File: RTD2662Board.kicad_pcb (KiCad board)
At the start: 2 copper layers, 100 x 65 mm, 227 parts, among them J1 USB_B, J10 Conn_Coaxial, J11 Conn_01x03, J2 AudioJack4, J3 Jack, J4 Conn_02x25_Odd_Even, J5 AudioJack4, J6 DVI_FEMALE, J7 HDMI_A_1.4, J8 Mini-DIN-4, J9 DB15_Female_HighDensity_Mount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, Q5 BC846, Q7 AO3401A, Q8 BC846, Q9 BC846, SW1 SW_Push, SW2 SW_Push, SW3 SW_Push, SW4 SW_Push, SW5 SW_Push, U1 TSOP382xx, U10 TPS61040DBV, U11 TPS61040DBV, U12 CH341T, U2 ES7134S, U4 PAM8003, U5 TPS61040DBV, U6 APW7313, U7 AMS1117-1.8, U8 RTD2662, U9 W25Qxx, Y1 Crystal, Y2 Crystal

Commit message: Revision 0.2
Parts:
- removed Q5: BC846, Package_TO_SOT_SMD:SOT-23
- removed R89: R, Resistor_SMD:R_0402_1005Metric_Pad0.72x0.64mm_HandSolder
- added C58: C, Capacitor_SMD:C_0402_1005Metric_Pad0.74x0.62mm_HandSolder, F.Cu at (112.2, 105.5)
- added C59: C, Capacitor_SMD:C_0402_1005Metric_Pad0.74x0.62mm_HandSolder, F.Cu at (106.2, 105.5)
- added C68: C, Capacitor_SMD:C_0402_1005Metric_Pad0.74x0.62mm_HandSolder, F.Cu at (133.0, 95.2)
- added C69: C, Capacitor_SMD:C_0402_1005Metric_Pad0.74x0.62mm_HandSolder, F.Cu at (130.2, 91.0)
- added C70: C, Capacitor_SMD:C_0402_1005Metric_Pad0.74x0.62mm_HandSolder, F.Cu at (132.2, 93.2)
- added C71: C, Capacitor_SMD:C_0402_1005Metric_Pad0.74x0.62mm_HandSolder, F.Cu at (131.5, 95.2)
- added C72: C, Capacitor_SMD:C_0402_1005Metric_Pad0.74x0.62mm_HandSolder, F.Cu at (36.5, 98.5)
- added C73: C, Capacitor_SMD:C_0402_1005Metric_Pad0.74x0.62mm_HandSolder, F.Cu at (87.5, 101.8)
- added C75: C, Capacitor_SMD:C_0402_1005Metric_Pad0.74x0.62mm_HandSolder, F.Cu at (36.5, 99.8)
- added C76: C, Capacitor_SMD:C_0402_1005Metric_Pad0.74x0.62mm_HandSolder, F.Cu at (87.6, 113.8)
- added C77: C, Capacitor_SMD:C_0402_1005Metric_Pad0.74x0.62mm_HandSolder, F.Cu at (36.4, 97.2)
- added C78: C, Capacitor_SMD:C_0402_1005Metric_Pad0.74x0.62mm_HandSolder, F.Cu at (36.4, 101.0)
- added C80: C, Capacitor_SMD:C_0402_1005Metric_Pad0.74x0.62mm_HandSolder, F.Cu at (78.2, 105.2)
- added D24: D_TVS, Inductor_SMD:L_0402_1005Metric_Pad0.77x0.64mm_HandSolder, F.Cu at (130.2, 88.0)
- added FB10: 120Ω, Inductor_SMD:L_0402_1005Metric_Pad0.77x0.64mm_HandSolder, F.Cu at (132.2, 87.2)
- added J12: Conn_02x06_Odd_Even, Connector_PinHeader_2.54mm:PinHeader_2x06_P2.54mm_Vertical, F.Cu at (127.0, 115.8)
- added J13: Conn_01x10, Connector_JST:JST_PH_B10B-PH-K_1x10_P2.00mm_Vertical, F.Cu at (56.8, 80.0)
- added J14: Conn_01x02, Connector_PinHeader_2.54mm:PinHeader_1x02_P2.54mm_Vertical, F.Cu at (144.8, 81.8)
- added J15: Conn_01x02, Connector_PinHeader_2.54mm:PinHeader_1x02_P2.54mm_Vertical, F.Cu at (75.2, 97.5)
- added JP5: Reset Pad, Jumper:SolderJumper-2_P1.3mm_Open_Pad1.0x1.5mm, F.Cu at (90.8, 118.8)
- added JP6: Power select, Connector_PinSocket_2.54mm:PinSocket_1x03_P2.54mm_Vertical, F.Cu at (60.0, 100.0)
- added JP7: Jump, Jumper:SolderJumper-2_P1.3mm_Bridged2Bar_RoundedPad1.0x1.5mm, B.Cu at (78.5, 92.0)
- added L8: L, Inductor_SMD:L_0402_1005Metric_Pad0.77x0.64mm_HandSolder, F.Cu at (132.2, 91.8)
- added Q1: AO3401A, Package_TO_SOT_SMD:SOT-23, F.Cu at (97.0, 79.0)
- added Q2: BC846, Package_TO_SOT_SMD:SOT-23, F.Cu at (101.5, 79.0)
- added R28: R, Resistor_SMD:R_0402_1005Metric_Pad0.72x0.64mm_HandSolder, F.Cu at (128.5, 90.2)
- added R30: R, Resistor_SMD:R_0402_1005Metric_Pad0.72x0.64mm_HandSolder, F.Cu at (127.0, 90.2)
- added R31: R, Resistor_SMD:R_0402_1005Metric_Pad0.72x0.64mm_HandSolder, F.Cu at (127.0, 93.2)
- added R36: R, Resistor_SMD:R_0402_1005Metric_Pad0.72x0.64mm_HandSolder, F.Cu at (128.5, 93.2)
- added R38: R, Resistor_SMD:R_0402_1005Metric_Pad0.72x0.64mm_HandSolder, F.Cu at (104.5, 80.0)
- added R40: R, Resistor_SMD:R_0402_1005Metric_Pad0.72x0.64mm_HandSolder, F.Cu at (132.2, 90.2)
- added R42: R, Resistor_SMD:R_0402_1005Metric_Pad0.72x0.64mm_HandSolder, F.Cu at (104.5, 78.2)
- added R78: 75Ω, Resistor_SMD:R_0402_1005Metric_Pad0.72x0.64mm_HandSolder, F.Cu at (132.2, 88.8)
- added R85: R, Resistor_SMD:R_0402_1005Metric_Pad0.72x0.64mm_HandSolder, F.Cu at (78.5, 87.0)
- added U3: AT24CS08-STUM, Package_TO_SOT_SMD:SOT-23-5, F.Cu at (127.8, 96.5)
- C52, C53, C54, C9: footprint Capacitor_SMD:C_0402_1005Metric_Pad0.74x0.62mm_HandSolder -> Capacitor_SMD:C_0805_2012Metric_Pad1.18x1.45mm_HandSolder
- JP1, JP2, JP3, JP4: moved to B.Cu
- R81: footprint Resistor_SMD:R_0402_1005Metric_Pad0.72x0.64mm_HandSolder -> Resistor_SMD:R_1210_3225Metric_Pad1.30x2.65mm_HandSolder
- SW1: value SW_Push -> POWER
- SW2: value SW_Push -> MENU
- SW3: value SW_Push -> UP
- SW4: value SW_Push -> DOWN
- SW5: value SW_Push -> SOURCE
- U9: footprint Package_SO:SOIC-8_3.9x4.9mm_P1.27mm -> Package_DIP:DIP-8_W7.62mm_Socket
- moved C9 24.0 mm to (55.8, 92.5), turned to 90 degrees
- moved R12 20.1 mm to (76.0, 87.0), turned to 90 degrees
- moved R20 18.6 mm to (71.0, 87.0), turned to 270 degrees
- moved R14 18.3 mm to (77.2, 87.0)
- moved R1 17.7 mm to (72.2, 87.0), turned to 90 degrees
- moved R8 17.7 mm to (74.8, 87.0), turned to 90 degrees
- moved R5 15.3 mm to (73.5, 87.0), turned to 90 degrees
- moved U7 13.5 mm to (61.5, 93.8)
- moved C39 13.0 mm to (94.2, 119.2), turned to 90 degrees
- moved R81 11.1 mm to (114.2, 84.5)
- moved JP3 10.0 mm to (92.8, 79.2), turned to 90 degrees
- moved JP4 9.80 mm to (92.8, 83.8)
- moved R9 9.63 mm to (120.6, 102.8), turned to 0 degrees
- moved R61 9.25 mm to (93.0, 119.2), turned to 270 degrees
- moved R76 8.68 mm to (103.5, 87.0)
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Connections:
- net CVBS+ renamed CVBS0+
- net CVBS- renamed CVBS0-
- net I2S_SDAT renamed I2S_SDAT0
- net Net-(U8-Pad114) renamed I2S_SDAT3
- net _CVBS+ renamed _CVBS0+
- net _CVBS- renamed _CVBS0-
- C50 pad 1: GND -> AVCC
- C51 pad 1: GND -> AVCC
- D21 pad 1: GND -> AVCC
- D22 pad 2: GND -> AVCC
- J1 pad 1: Net-(J1-Pad1) -> VUSB
- J4 pad 49: Net-(J4-Pad49) -> EN_LCD
- J4 pad 50: Net-(J4-Pad50) -> EN_BL
- JP3 pad 1: +3V3 -> Net-(JP3-Pad1)
- Q7 pad 3: Net-(J3-Pad1) -> Net-(JP6-Pad2)
- R1 pad 1: Net-(R1-Pad1) -> BUTTONS
- R1 pad 2: GND -> MENUB
- R10 pad 1: RED_LED -> GRN_LED
- R12 pad 1: Net-(R12-Pad1) -> BUTTONS
- R12 pad 2: GND -> SRCB
- R13 pad 1: GRN_LED -> RED_LED
- R14 pad 1: +3V3 -> Net-(J13-Pad9)
- R14 pad 2: Net-(Q5-Pad3) -> RED_LED
- R17 pad 1: Net-(Q5-Pad1) -> Net-(C73-Pad1)
- R5 pad 1: Net-(R5-Pad1) -> BUTTONS
- R5 pad 2: GND -> UPB
- R8 pad 1: Net-(R8-Pad1) -> BUTTONS
- R8 pad 2: GND -> DWNB
- R88 pad 1: EN_REF -> EN_LCD
- SW1 pad 1: Net-(R1-Pad1) -> GND
- SW2 pad 1: Net-(R5-Pad1) -> GND
- SW2 pad 2: BUTTONS -> MENUB
- SW3 pad 1: Net-(R8-Pad1) -> GND
- SW3 pad 2: BUTTONS -> UPB
- SW4 pad 1: Net-(R12-Pad1) -> GND
- SW4 pad 2: BUTTONS -> DWNB
- SW5 pad 2: BUTTONS -> SRCB
- U10 pad 4: EN_REF -> EN_LCD
- U11 pad 4: EN_REF -> EN_LCD
- U4 pad 12: Net-(Q5-Pad3) -> Net-(C73-Pad1)
- U4 pad 2: Net-(J2-PadS) -> Net-(J2-PadR2)
- U8 pad 100: VOL -> EN_LCD
- U8 pad 102: Net-(U8-Pad102) -> VOL
- U8 pad 112: Net-(U8-Pad112) -> I2S_SDAT1
- U8 pad 113: Net-(U8-Pad113) -> I2S_SDAT2
- U8 pad 47: Net-(U8-Pad47) -> CVBS1+
- U8 pad 48: Net-(U8-Pad48) -> CVBS1-
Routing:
- net GND: track 682.3 -> 26.4 mm, vias 308 -> 16
- net +1V8: track 146.8 -> 41.3 mm, vias 5 -> 0
- net IRDA: track 79.7 -> 13.9 mm, vias 2 -> 0
- net VCOM: track 32.3 -> 97.2 mm, vias 0 -> 2
- net BUTTONS: track 102.6 -> 39.7 mm
- net TX: track 116.2 -> 56.6 mm
- net RX: track 124.3 -> 65.4 mm
- net +3V3: track 398.9 -> 358.7 mm
- net EN_LCD: track 0.00 -> 36.9 mm
- net I2S_SDAT1: track 0.00 -> 35.5 mm, vias 0 -> 1
- net CVBS1+: track 0.00 -> 34.9 mm
- net EIO6: track 0.00 -> 34.0 mm, vias 0 -> 1
- net CVBS1-: track 0.00 -> 33.5 mm
- net I2S_SDAT2: track 0.00 -> 33.0 mm, vias 0 -> 1
- net EIO7: track 0.00 -> 31.4 mm, vias 0 -> 1
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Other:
- board size 100 x 65 mm -> 100 x 70 mm
- net class LCD Signal removed
- net class Power added: clearance 0.2, trace_width 0.75, via_dia 0.8, via_drill 0.4

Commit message: Revision 1.0
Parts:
- removed C78, C80: C, Capacitor_SMD:C_0402_1005Metric_Pad0.74x0.62mm_HandSolder
- removed the J6 at (90.2, 142.5)
- removed the R9 at (120.6, 102.8)
- removed the U9 at (83.5, 118.2)
- added C65: C, Capacitor_SMD:C_0402_1005Metric_Pad0.74x0.62mm_HandSolder, F.Cu at (78.2, 104.8)
- added J1: DVI_Female, RTD2662Board:DVI, F.Cu at (90.2, 142.5)
- added R57: R, Resistor_SMD:R_0402_1005Metric_Pad0.72x0.64mm_HandSolder, F.Cu at (125.0, 84.8)
- added R87: R, Resistor_SMD:R_0402_1005Metric_Pad0.72x0.64mm_HandSolder, F.Cu at (62.8, 119.5)
- added U10: W25Qxx, RTD2662Board:SOIC-8_3.9x4.9mm_P1.27mm_DIP-8_W7.62mm_Socket, F.Cu at (79.6, 113.2)
- D22: renamed from D2; value LED_Dual_ACAC -> Dual LED
- J10: renamed from J11; value Conn_01x03 -> UART/I2C
- J11: renamed from J4; value Conn_02x25_Odd_Even -> LCD Connector
- J12: renamed from J15; value Conn_01x02 -> SPDIFF
- J15: renamed from J12; value Conn_02x06_Odd_Even -> Expansion Connector
- J9: renamed from J13; value Conn_01x10 -> Keyboard Connector
- JP4: footprint Jumper:SolderJumper-2_P1.3mm_Bridged2Bar_RoundedPad1.0x1.5mm -> Jumper:SolderJumper-2_P1.3mm_Open_RoundedPad1.0x1.5mm
- moved C61 91.3 mm to (127.8, 97.8)
- moved C64 52.6 mm to (88.5, 90.0), turned to 180 degrees
- moved JP7 44.9 mm to (58.8, 87.2), turned to 180 degrees
- moved C69 43.9 mm to (64.2, 87.2)
- moved R84 42.2 mm to (65.5, 87.2)
- moved C62 31.9 mm to (67.2, 108.2)
- moved R77 27.5 mm to (78.5, 90.0), turned to 270 degrees
- moved R80 25.0 mm to (77.2, 90.0), turned to 270 degrees
- moved REF** 13.5 mm to (52.8, 96.2)
- moved Q4 9.36 mm to (100.0, 88.2)
- moved C37 9.33 mm to (109.8, 86.8)
- moved C38 9.33 mm to (108.2, 86.8)
- moved C43 9.33 mm to (121.0, 86.8)
- moved C44 9.33 mm to (122.5, 86.8)
- moved D17 9.33 mm to (108.2, 89.2)
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- renumbered C36 to C1, C17 to C10, C69 to C11, C70 to C12, C19 to C13, C20 to C14, C71 to C15, C22 to C16, C26 to C17, C28 to C18, C31 to C19, C12 to C2, C30 to C20, C29 to C21, C32 to C22, C27 to C23, C16 to C24, C35 to C25, C18 to C26, C34 to C27, C21 to C28, C33 to C29, C41 to C3, C23 to C30, C45 to C31, C24 to C32, C43 to C33, C25 to C34, C40 to C35, C46 to C36, C47 to C37, C48 to C38, C52 to C39, C42 to C4, C37 to C40, C38 to C41, C49 to C42, C50 to C43, C51 to C44, C53 to C45, C1 to C46, C2 to C47, C4 to C48, C5 to C49, C13 to C5, C3 to C50, C54 to C51, C73 to C52, C6 to C53, C57 to C54, C60 to C55, C63 to C56, C64 to C57, C65 to C58, C66 to C59, C14 to C6, C67 to C60, C72 to C61, C75 to C62, C76 to C63, C77 to C64, C7 to C66, C8 to C67, C9 to C68, C39 to C69, C44 to C7, C55 to C70, C56 to C71, C59 to C72, C58 to C73, C62 to C74, C61 to C75, C10 to C76, C11 to C77, C15 to C8, C68 to C9, D12 to D1, D13 to D10, D14 to D11, D15 to D12, D16 to D13, D17 to D14, D20 to D15, D18 to D16, D19 to D17, D1 to D18, D21 to D19, D4 to D2, D22 to D20, D23 to D21, D11 to D23, D3 to D24, D24 to D3, D6 to D4, D9 to D5, D8 to D6, D5 to D7, D10 to D8, D7 to D9, FB8 to FB1, FB9 to FB10, FB1 to FB2, FB10 to FB3, FB3 to FB4, FB2 to FB7, FB7 to FB8, FB4 to FB9, J2 to J13, J3 to J14, J7 to J2, J5 to J3, J9 to J4, J10 to J5, J14 to J6, J8 to J7, J1 to J8, JP7 to JP5, JP5 to JP7, L5 to L1, L3 to L2, L8 to L3, L6 to L5, L1 to L6, L2 to L8, Q8 to Q1, Q9 to Q2, Q1 to Q3, Q2 to Q4, Q7 to Q5, R2 to R1, R34 to R10, R40 to R11, R37 to R12, R78 to R13, R41 to R14, R7 to R15, R15 to R16, R21 to R17, R27 to R18, R48 to R19, R4 to R2, R47 to R20, R49 to R21, R53 to R22, R57 to R23, R55 to R24, R54 to R25, R58 to R26, R52 to R27, R35 to R28, R64 to R29, R32 to R3, R39 to R30, R62 to R31, R43 to R32, R59 to R33, R50 to R34, R51 to R35, R44 to R36, R70 to R37, R56 to R38, R45 to R39, R16 to R4, R69 to R40, R46 to R41, R67 to R42, R71 to R43, R72 to R44, R63 to R45, R18 to R46, R73 to R47, R74 to R48, R76 to R49, R19 to R5, R77 to R50, R88 to R51, R60 to R52, R20 to R53, R75 to R54, R66 to R55, R1 to R56, R81 to R58, R11 to R59, R29 to R6, R5 to R60, R3 to R61, R8 to R62, R6 to R63, R79 to R64, R12 to R65, R82 to R66, R38 to R67, R14 to R68, R17 to R69, R65 to R7, R42 to R70, R80 to R71, R83 to R72, R84 to R73, R85 to R74, R28 to R75, R30 to R76, R10 to R77, R31 to R78, R36 to R79, R33 to R8, R13 to R80, R22 to R81, R23 to R82, R24 to R83, R61 to R84, R25 to R85, R26 to R86, R68 to R9, U8 to U1, U6 to U11, U7 to U12, U10 to U2, U1 to U3, U12 to U4, U2 to U6, U4 to U7, U11 to U8, U3 to U9, Y2 to Y1, Y1 to Y2
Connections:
- net Net-(C39-Pad1) renamed ~RESET~
- net Net-(J2-PadR1) renamed RIGHT+
- net Net-(J2-PadR2) renamed LEFT-
- net Net-(J2-PadS) renamed RIGHT-
- net Net-(J2-PadT) renamed LEFT+
- C11 pad 2: _CVBS1- -> GND
- C12 pad 2: _CVBS1- -> GND
- C13 pad 2: _S_Y- -> GND
- C14 pad 2: _S_Y- -> GND
- C15 pad 2: _CVBS1- -> GND
- C16 pad 2: _S_Y- -> GND
- C20 pad 2: _B_Pb- -> GND
- C21 pad 1: _VGA_R- -> GND
- C26 pad 2: _B_Pb- -> GND
- C27 pad 1: _VGA_G- -> GND
- C3 pad 2: _CVBS0- -> GND
- C32 pad 2: _B_Pb- -> GND
- C33 pad 1: _VGA_B- -> GND
- C4 pad 2: _CVBS0- -> GND
- C5 pad 2: _S_C- -> GND
- C6 pad 2: _S_C- -> GND
- C7 pad 2: _CVBS0- -> GND
- C8 pad 2: _S_C- -> GND
- D1 pad 2: _CVBS0- -> GND
- D10 pad 2: _VGA_B- -> GND
- D2 pad 2: _S_C- -> GND
- D3 pad 2: _CVBS1- -> GND
- D4 pad 2: _S_Y- -> GND
- D5 pad 2: _B_Pb- -> GND
- D6 pad 2: _VGA_R- -> GND
- D7 pad 2: _B_Pb- -> GND
- D8 pad 2: _VGA_G- -> GND
- D9 pad 2: _B_Pb- -> GND
- J11 pad 45: +1V8 -> +3V3
- J12 pad 1: I2S_SDAT1 -> I2S_SDAT3
- J4 pad 6: _VGA_R- -> GND
- J4 pad 7: _VGA_G- -> GND
- J4 pad 8: _VGA_B- -> GND
- J5 pad 2: _CVBS0- -> GND
- J6 pad 2: _CVBS1- -> GND
- J7 pad 1: _S_Y- -> GND
- J7 pad 2: _S_C- -> GND
- JP2 pad 2: _B_Pb- -> GND
- R10 pad 2: _S_C- -> GND
- R13 pad 2: _CVBS1- -> GND
- R14 pad 2: _S_Y- -> GND
- R24 pad 2: _B_Pb- -> GND
- R25 pad 2: _VGA_R- -> GND
- R26 pad 2: _B_Pb- -> GND
- R27 pad 2: _VGA_R- -> GND
- R30 pad 2: _B_Pb- -> GND
- R31 pad 2: _VGA_G- -> GND
- R32 pad 2: _B_Pb- -> GND
- R33 pad 2: _VGA_G- -> GND
- R39 pad 2: _B_Pb- -> GND
- R40 pad 2: _VGA_B- -> GND
- R41 pad 2: _B_Pb- -> GND
- R42 pad 2: _VGA_B- -> GND
- R9 pad 2: _CVBS0- -> GND
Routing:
- net GND: track 26.4 -> 248.4 mm, vias 16 -> 320
- net +1V8: track 41.3 -> 158.5 mm, vias 0 -> 6
- net +3V3: track 358.7 -> 461.7 mm, vias 19 -> 24
- net ~RESET~: track 4.86 -> 102.2 mm, vias 0 -> 6
- net TX: track 56.6 -> 147.5 mm, vias 3 -> 6
- net RX: track 65.4 -> 154.4 mm, vias 3 -> 6
- net BUTTONS: track 39.7 -> 123.4 mm
- net IRDA: track 13.9 -> 94.2 mm, vias 0 -> 1
- net VCOM: track 97.2 -> 36.3 mm, vias 2 -> 1
- net I2S_SDAT3: track 0.00 -> 47.0 mm, vias 0 -> 2
- net _CVBS0-: track 42.5 -> 0.00 mm
- net _B_Pb-: track 36.0 -> 0.00 mm, vias 3 -> 0
- net GRN_LED: track 70.4 -> 34.6 mm
- net I2S_SDAT2: track 33.0 -> 67.2 mm, vias 1 -> 3
- net RED_LED: track 68.7 -> 35.2 mm
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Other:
- rule pad_to_mask_clearance: 0 -> 0.05
- board text added: "+3.3V"
- board text added: "1-2 - 3.3V 3-2 - 12V/5V"
- board text added: "AUDIO"
- board text added: "AVCC"
- board text added: "B1/B7/O3+"
- board text added: "B2"
- board text added: "B3"
- board text added: "B4"
- board text added: "B5"
- board text added: "B6"
- board text added: "B7"
- board text added: "BL_ANO"
- board text added: "BL_CAT"
- board text added: "CVBS1"
- board text added: "CVBS2+"
- board text added: "CVBS2-"
- board text added: "DCK"
- board text added: "DEN/E0+"
- board text added: "DVCC"
- board text added: "DVI"
- board text added: "DVS"
- board text added: "E0-/DHS"
- board text added: "E1-/R2/R0"
- board text added: "E2-/R4/R2"
- board text added: "E3-/G2/R6"
- board text added: "EC-/R6/R4"
- board text added: "EN_BL"
- board text added: "EN_LCD"
- board text added: "G1/G5/E0+"
- board text added: "G3/G7/O1+"
- board text added: "G5/B3/O2+"
- board text added: "G7/B5/OC+"
- board text added: "GND"
- board text added: "HDMI"
- board text added: "HMIR"
- board text added: "IO0"
- board text added: "IO1"
- board text added: "IO2"
- board text added: "IO3"
- board text added: "IO4"
- board text added: "IO5"
- board text added: "IO6"
- board text added: "IO7"
- board text added: "IO8"
- board text added: "IO9"
- board text added: "IR"
- board text added: "JACK PWR"
- board text added: "JP1 & JP2: 1-2 - GND-SLEEVE 3-2 - GND-RING2"
- board text added: "LEDA1"
- board text added: "LEDA2"
- board text added: "O-5V C-12V"
- board text added: "O0-/G4/G0"
- board text added: "O1-/G6/G2"
- board text added: "O2-/B2/G4"
- board text added: "O3-/B6/B0"
- board text added: "OC-/B4/G6"
- board text added: "ORTD2662-PROTOBOARD-REV1"
- board text added: "R1/R3/E1+"
- board text added: "R3/R5/E2+"
- board text added: "R5/R7/EC+"
- board text added: "R7/G3/E3+"
- board text added: "RESET"
- board text added: "RGsB YPbPr"
- board text added: "RX/SCL"
- board text added: "S/PDIF"
- board text added: "SVIDEO"
- board text added: "TX/SDA"
- board text added: "USB PWR"
- board text added: "VCOM"
- board text added: "VGA"
- board text added: "VGH"
- board text added: "VGL"
- board text added: "VMIR"

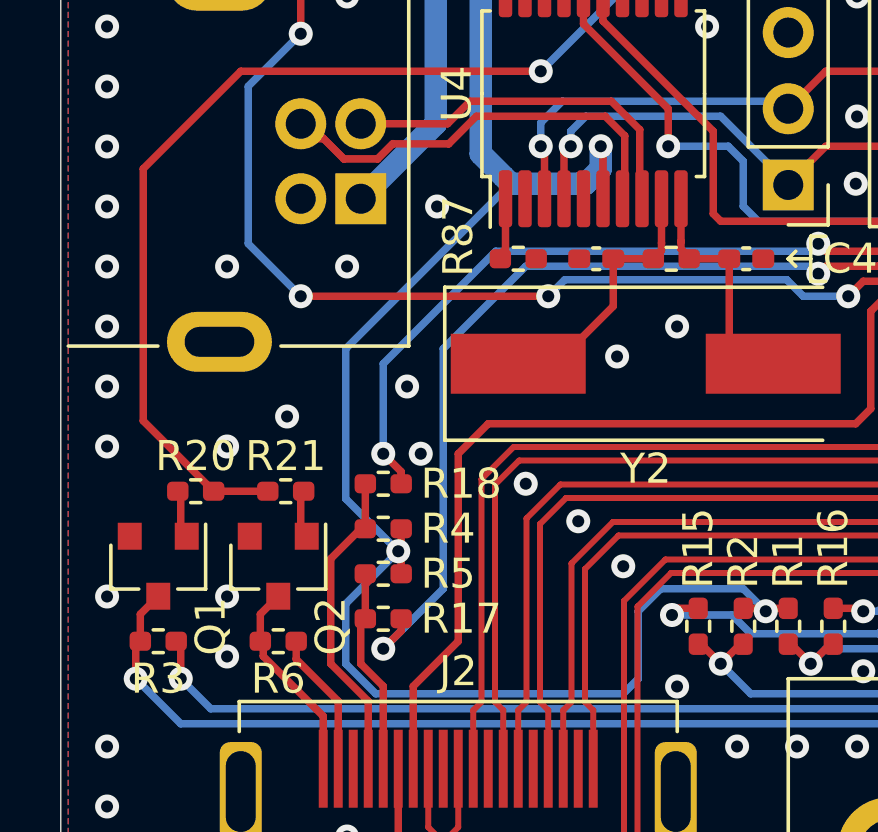
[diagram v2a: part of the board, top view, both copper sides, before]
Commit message: Added CEC pullup
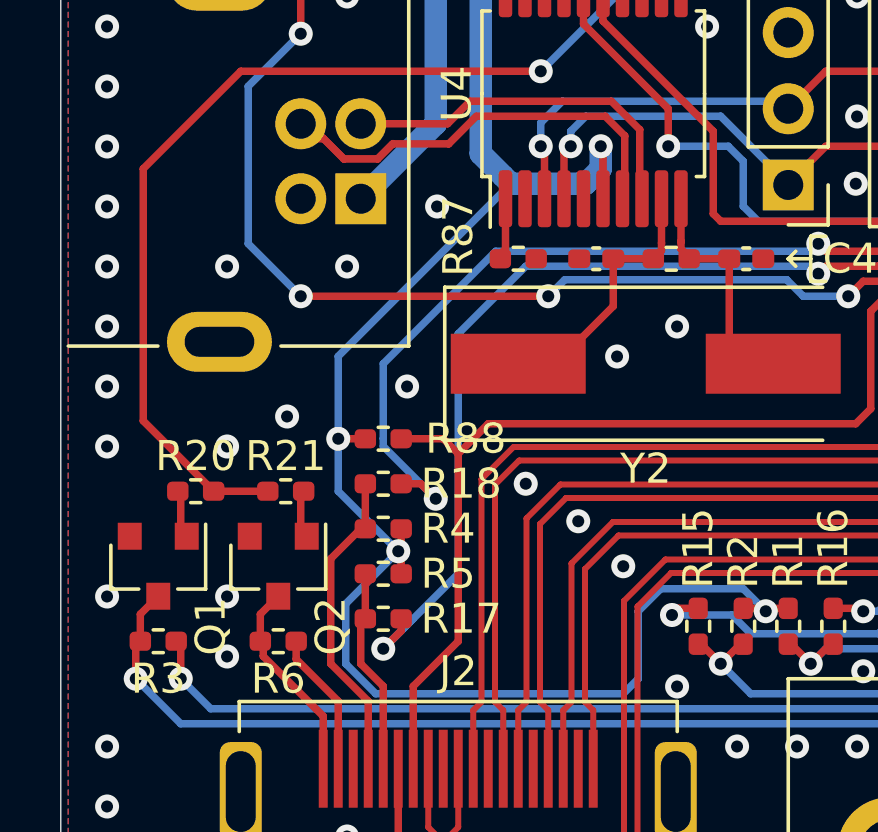
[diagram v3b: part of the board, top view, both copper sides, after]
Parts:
- added R88: 47kΩ, Resistor_SMD:R_0402_1005Metric_Pad0.72x0.64mm_HandSolder, F.Cu at (58.2, 125.5)
- C1, C10, C15, C16, C2, C7, C8, C9: value C -> 22nF
- C11, C13, C3, C5: value C -> 33pF
- C12, C14, C4, C6: value C -> 82pF
- C17, C18, C19, C22, C23, C24, C25, C28, C29, C30, C31, C34, C35: value C -> 47nF
- C20, C21, C26, C27, C32, C33: value C -> 5.1pF
- C36, C42, C69, C77: value C -> 100nF
- C37, C38, C43, C44, C50, C52, C54, C55, C56, C57, C58, C59, C60, C61, C62, C63, C64, C65, C70, C71, C72, C73, C74, C75: value C -> 1uF
- C39, C45, C51, C66: value C -> 10uF
- C40, C41: value C -> 20pF
- C46, C47: value C -> 2.2uF
- C48, C49: value C -> 15pF
- C53: value C -> 10nF
- C67, C68: value C -> 22uF
- C76: value C -> 3.9nF
- D1, D10, D11, D12, D13, D14, D2, D3, D4, D5, D6, D7, D8, D9: value D_TVS -> LXES03AAA1
- D15, D18, D21: value D_Schottky -> MBR0530
- D17: value 00.0V -> 6.8V
- D20: value 00.0V -> 16V
- D22: value Dual LED -> R/G Dual LED
- D23: value D -> BAT42WS
- D24: value Zener -> 4.7V
- J1: value DVI_Female -> DVI
- J13, J3: value AudioJack4 -> 3.5mm jack
- J14: value Jack -> DC Jack
- J2: value HDMI_A_1.4 -> HDMI-A
- J4: value DB15_Female_HighDensity_MountingHoles -> VGA
- J6: value Conn_01x02 -> CVBS2 In
- J8: value USB_B -> USB B
- JP1, JP2: value Jumper -> Ring3/Sleeve GND Select
- JP5: value Jump -> Common negative jumper
- L1, L2, L3, L4: value L -> 8.2uH
- L5, L6, L7: value L -> 10uF
- L8: value L -> 10uH
- R1, R2, R34, R35, R4, R47, R48, R5, R75, R76: value R -> 4.7kΩ
- R10, R14: value 75 -> 75Ω
- R11, R12, R68, R7, R74, R77, R8, R80: value R -> 330Ω
- R15, R16, R17, R18, R19, R22, R23, R26, R27, R28, R29, R32, R33, R36, R37, R38, R41, R42, R43, R44, R45, R46, R54, R78, R79: value R -> 100Ω
- R20, R21, R3, R51, R57, R6, R67, R70, R84: value R -> 10kΩ
- R49: value R -> 82kΩ
- R50, R66: value R -> 11kΩ
- R52, R59: value R -> 1MΩ
- R53, R55, R69: value R -> 1kΩ
- R56: value R -> 270Ω
- R58: value R -> 6.8Ω
- R60: value R -> 680Ω
- R61, R63: value R -> 470Ω
- R62: value R -> 1.5kΩ
- R64: value R -> 15kΩ
- R65: value R -> 3.9kΩ
- R71, R83: value R -> 6.8kΩ
- R72: value R -> 2kΩ
- R73: value R -> 3.6kΩ
- R81: value R -> 100kΩ
- R85: value R -> 10k
- R87: value R -> 2.2kΩ
- RN1, RN2: value R_Pack04 -> 100Ω
- RV1: value R_POT -> 10kΩ
- Y1: value Crystal -> 27MHz
- Y2: value Crystal -> 12MHz
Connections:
- J1 pad 12: Net-(J1-Pad12) -> (no net)
- J1 pad 13: Net-(J1-Pad13) -> (no net)
- J1 pad 20: Net-(J1-Pad20) -> (no net)
- J1 pad 21: Net-(J1-Pad21) -> (no net)
- J1 pad 4: Net-(J1-Pad4) -> (no net)
- J1 pad 5: Net-(J1-Pad5) -> (no net)
- J1 pad 8: Net-(J1-Pad8) -> (no net)
- J1 pad C1: Net-(J1-PadC1) -> (no net)
- J1 pad C2: Net-(J1-PadC2) -> (no net)
- J1 pad C3: Net-(J1-PadC3) -> (no net)
- J1 pad C4: Net-(J1-PadC4) -> (no net)
- J11 pad 10: Net-(J11-Pad10) -> (no net)
- J11 pad 8: Net-(J11-Pad8) -> (no net)
- J11 pad 9: Net-(J11-Pad9) -> (no net)
- J4 pad 11: Net-(J4-Pad11) -> (no net)
- J4 pad 4: Net-(J4-Pad4) -> (no net)
- J4 pad 9: Net-(J4-Pad9) -> (no net)
- U1 pad 28: Net-(U1-Pad28) -> (no net)
- U1 pad 39: Net-(U1-Pad39) -> (no net)
- U4 pad 14: Net-(U4-Pad14) -> (no net)
- U4 pad 17: Net-(U4-Pad17) -> (no net)
- U4 pad 18: Net-(U4-Pad18) -> (no net)
- U4 pad 2: Net-(U4-Pad2) -> (no net)
- U4 pad 5: Net-(U4-Pad5) -> (no net)
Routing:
- net HDMI_SDA: track 44.1 -> 46.4 mm
- net CEC: track 51.0 -> 52.9 mm
- net +3V3: track 461.7 -> 462.8 mm, vias 24 -> 25
- net GND: vias 320 -> 319

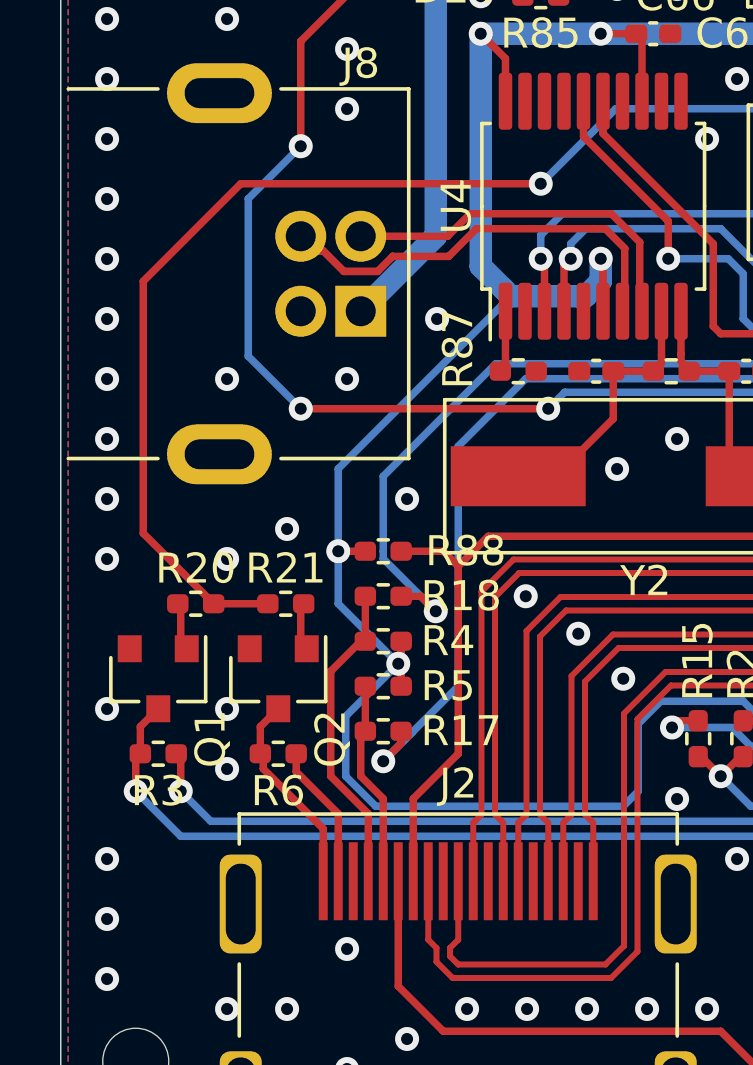
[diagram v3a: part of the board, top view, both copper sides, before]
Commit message: Added pull-ups to HPD transistors.
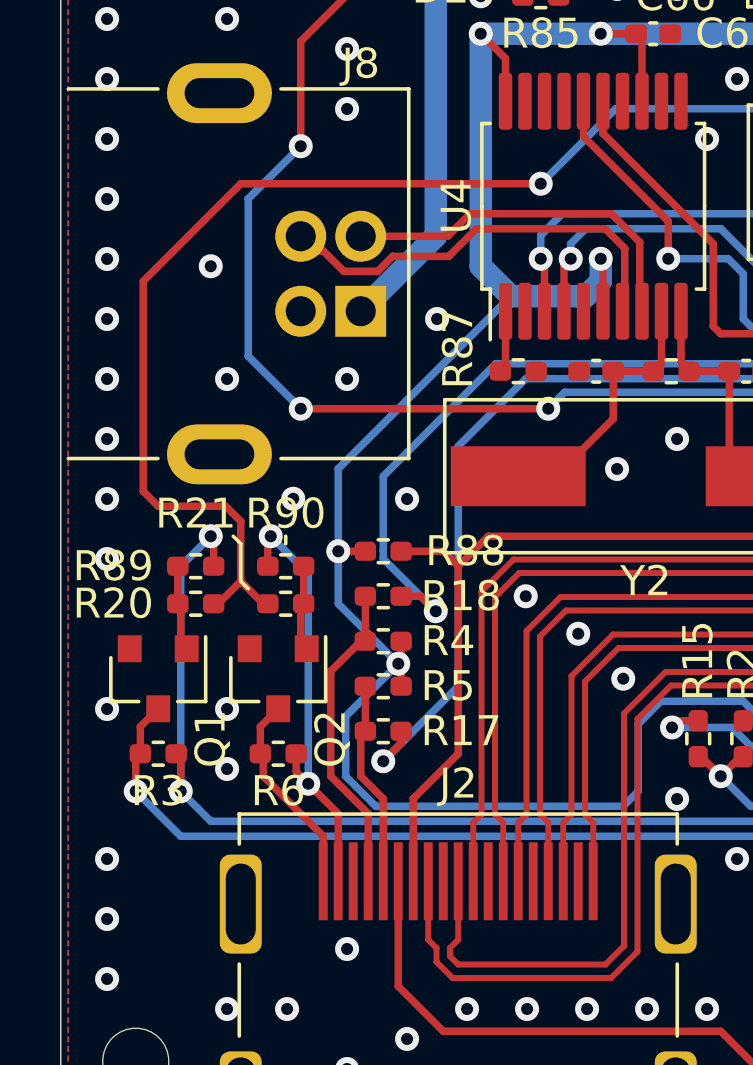
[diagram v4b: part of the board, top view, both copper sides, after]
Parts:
- added R89: 10kΩ, Resistor_SMD:R_0402_1005Metric_Pad0.72x0.64mm_HandSolder, F.Cu at (52.0, 126.0)
- added R90: 10kΩ, Resistor_SMD:R_0402_1005Metric_Pad0.72x0.64mm_HandSolder, F.Cu at (55.0, 126.0)
- R20, R21, R3, R6: value 10kΩ -> 1kΩ
- turned R3 to 0 degrees
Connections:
- R3 pad 1: Net-(J1-Pad14) -> Net-(J1-Pad16)
- R3 pad 2: Net-(J1-Pad16) -> Net-(J1-Pad14)
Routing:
- net Net-(J1-Pad14): track 41.6 -> 51.5 mm, vias 1 -> 2
- net Net-(J2-Pad18): track 4.83 -> 14.6 mm, vias 0 -> 2
- net HPD: track 66.9 -> 68.5 mm
- net Net-(Q2-Pad1): track 1.45 -> 2.76 mm
- net Net-(Q1-Pad1): track 1.64 -> 2.80 mm
